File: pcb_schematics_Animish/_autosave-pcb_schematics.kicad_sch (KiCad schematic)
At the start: 73 parts, among them J1 CUE_SJ1-352XNG, J2 Conn_01x01_Pin, J3 Conn_01x05, J4 Conn_01x05, J5 Conn_01x05, SW1 SW_Push, U1 RPi_Pico_TH, U2 RDA5807M_Module, U3 LM386, U4 LM386

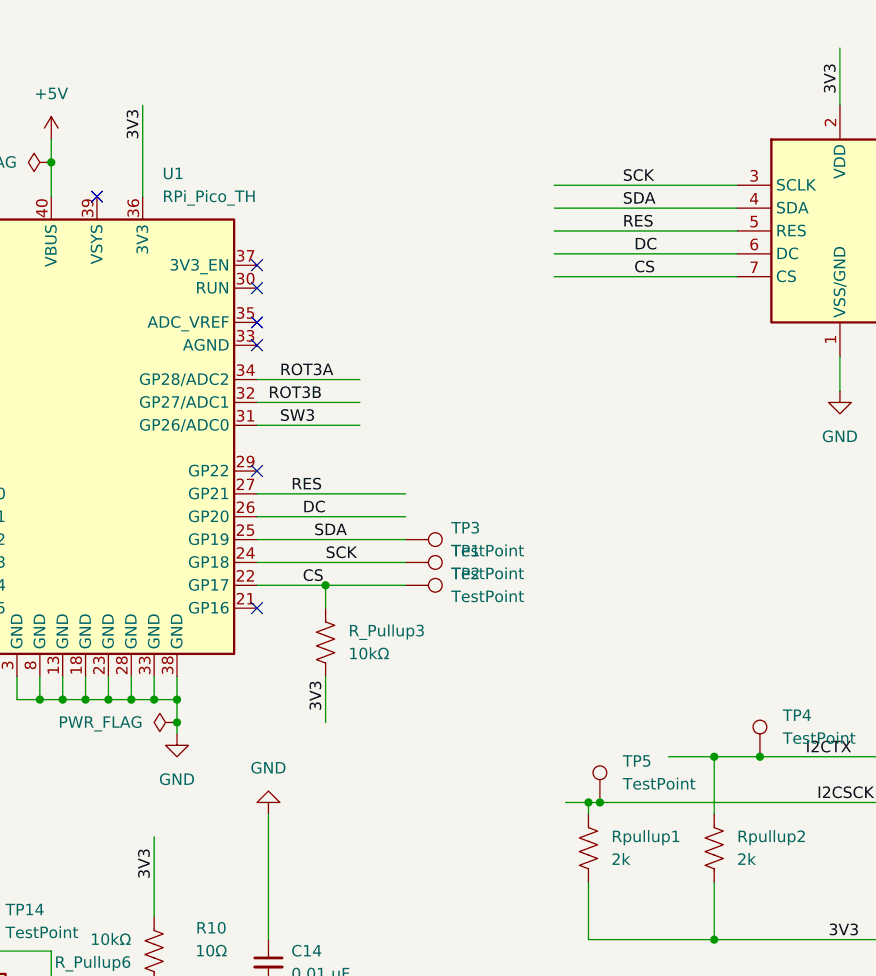
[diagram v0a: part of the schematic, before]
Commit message: Submitted to JLCPCB
Modification with pcb_schematics being the final version.
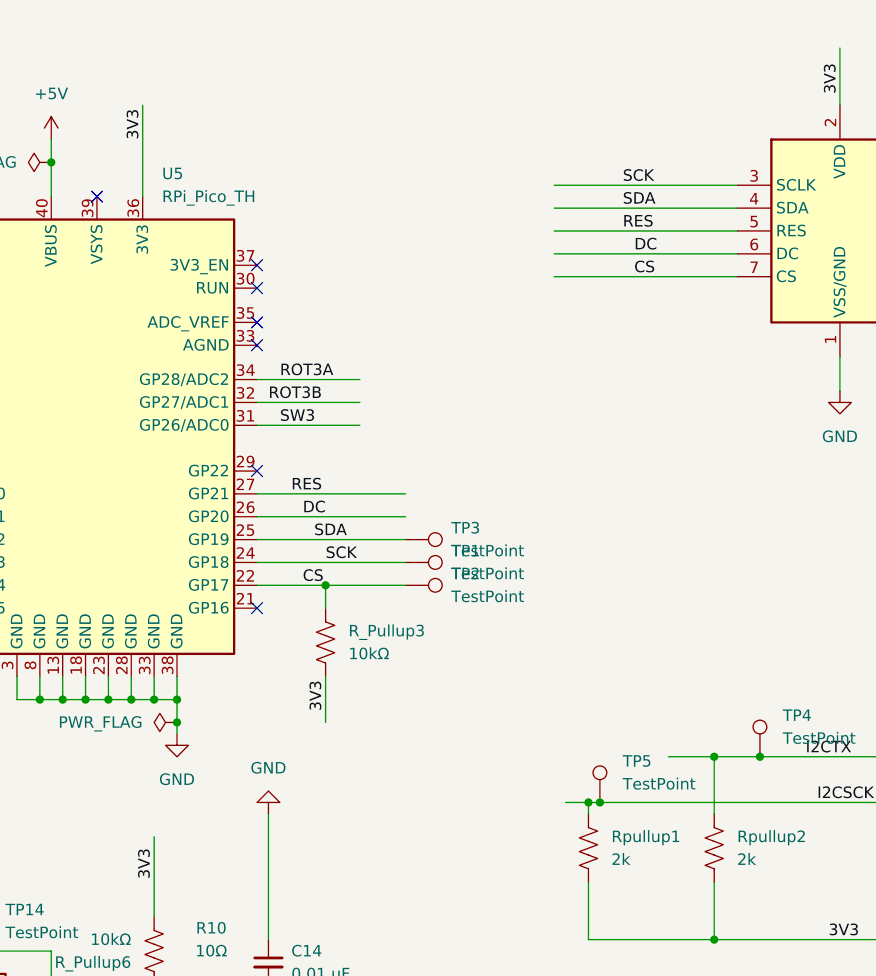
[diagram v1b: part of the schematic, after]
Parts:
- removed U1: RPi_Pico_TH, Module:RaspberryPi_Pico_Common_THT, symbol ECE:RPi_Pico_TH
- added U5: RPi_Pico_TH, ECE:RPi_Pico_TH, symbol ECE:RPi_Pico_TH
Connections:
- net +5V: now also U5.40 (VBUS)
- net 3V3: now also U5.36 (3V3)
- net CS: now also U5.22 (GP17)
- net DC: now also U5.26 (GP20)
- net GND: now also U5.13 (GND), U5.18 (GND), U5.23 (GND), U5.28 (GND), U5.3 (GND), U5.33 (AGND), U5.38 (GND), U5.8 (GND)
- net I2CSCK: now also U5.20 (GP15)
- net I2CTX: now also U5.19 (GP14)
- net RES: now also U5.27 (GP21)
- net ROT1A: now also U5.5 (GP3)
- net ROT1B: now also U5.4 (GP2)
- net ROT2A: now also U5.9 (GP6)
- net ROT2B: now also U5.10 (GP7)
- net ROT3A: now also U5.34 (GP28/ADC2)
- net ROT3B: now also U5.32 (GP27/ADC1)
- net SCK: now also U5.24 (GP18)
- net SDA: now also U5.25 (GP19)
- net SW1: now also U5.1 (GP0)
- net SW2: now also U5.2 (GP1)
- net SW3: now also U5.31 (GP26/ADC0)
- net SW4: now also U5.7 (GP5)
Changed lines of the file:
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@@
 	(wire
 		(pts
-			(xy 114.3 101.6) (xy 114.3 95.25)
+			(xy 114.3 95.25) (xy 114.3 101.6)
 		)
 		(stroke
@@
 	)
 	(symbol
-		(lib_id "ECE:RPi_Pico_TH")
-		(at 45.72 59.69 0)
-		(unit 1)
-		(exclude_from_sim no)
-		(in_bom yes)
-		(on_board yes)
-		(dnp no)
-		(fields_autoplaced yes)
-		(property "Reference" "U1"
-			(at 52.9941 30.48 0)
-			(effects
-				(font
-					(size 1.27 1.27)
-				)
-				(justify left)
-			)
-		)
-		(property "Value" "RPi_Pico_TH"
-			(at 52.9941 33.02 0)
-			(effects
-				(font
-					(size 1.27 1.27)
-				)
-				(justify left)
-			)
-		)
-		(property "Footprint" "Module:RaspberryPi_Pico_Common_THT"
-			(at 45.72 63.5 0)
-			(effects
-				(font
-					(size 1.27 1.27)
-				)
-				(hide yes)
-			)
-		)
-		(property "Datasheet" ""
-			(at 45.72 62.23 0)
-			(effects
-				(font
-					(size 1.27 1.27)
-				)
-				(hide yes)
-			)
-		)
-		(property "Description" ""
-			(at 45.72 59.69 0)
-			(effects
-				(font
-					(size 1.27 1.27)
-				)
-			)
-		)
-		(pin "34"
-		)
-		(pin "38"
-		)
-		(pin "2"
-		)
-		(pin "33"
-		)
-		(pin "37"
-		)
-		(pin "22"
-		)
-		(pin "21"
-		)
-		(pin "6"
-		)
-		(pin "8"
-		)
-		(pin "27"
-		)
-		(pin "20"
-		)
-		(pin "11"
-		)
-		(pin "25"
-		)
-		(pin "30"
-		)
-		(pin "9"
-		)
-		(pin "32"
-		)
-		(pin "33"
-		)
-		(pin "35"
-		)
-		(pin "12"
-		)
-		(pin "36"
-		)
-		(pin "31"
-		)
-		(pin "23"
-		)
-		(pin "28"
-		)
-		(pin "29"
-		)
-		(pin "5"
-		)
-		(pin "16"
-		)
-		(pin "13"
-		)
-		(pin "15"
-		)
-		(pin "39"
-		)
-		(pin "4"
-		)
-		(pin "3"
-		)
-		(pin "40"
-		)
-		(pin "17"
-		)
-		(pin "24"
-		)
-		(pin "26"
-		)
-		(pin "19"
-		)
-		(pin "1"
-		)
-		(pin "10"
-		)
-		(pin "18"
-		)
-		(pin "7"
-		)
-		(pin "14"
-		)
-		(instances
-			(project "pcb_schematics"
-				(path "/a6913523-cf8b-4e29-b403-fe0fb62af3ee"
-					(reference "U1")
-					(unit 1)
-				)
-			)
-		)
-	)
-	(symbol
 		(lib_id "Device:C_Small")
 		(at 233.68 102.87 0)
@@
 					(unit 1)
 				)
+			)
+		)
+	)
+	(symbol
+		(lib_name "RPi_Pico_TH_1")
+		(lib_id "ECE:RPi_Pico_TH")
+		(at 45.72 59.69 0)
+		(unit 1)
+		(exclude_from_sim no)
+		(in_bom yes)
+		(on_board yes)
+		(dnp no)
+		(fields_autoplaced yes)
+		(property "Reference" "U5"
+			(at 52.9433 30.48 0)
+			(effects
+				(font
+					(size 1.27 1.27)
+				)
+				(justify left)
+			)
+		)
+		(property "Value" "RPi_Pico_TH"
+			(at 52.9433 33.02 0)
+			(effects
+				(font
+					(size 1.27 1.27)
+				)
+				(justify left)
+			)
+		)
+		(property "Footprint" "ECE:RPi_Pico_TH"
+			(at 45.72 63.5 0)
+			(effects
+				(font
+					(size 1.27 1.27)
+				)
+				(hide yes)
+			)
+		)
+		(property "Datasheet" ""
+			(at 45.72 62.23 0)
+			(effects
+				(font
+					(size 1.27 1.27)
+				)
+				(hide yes)
+			)
+		)
+		(property "Description" "Raspberry Pi Pico"
+			(at 45.72 59.69 0)
+			(effects
+				(font
+					(size 1.27 1.27)
+				)
+				(hide yes)
+			)
+		)
+		(pin "6"
+		)
+		(pin "11"
+		)
+		(pin "2"
+		)
+		(pin "13"
+		)
+		(pin "19"
+		)
+		(pin "17"
+		)
+		(pin "33"
+		)
+		(pin "5"
+		)
+		(pin "7"
+		)
+		(pin "12"
+		)
+		(pin "9"
+		)
+		(pin "14"
+		)
+		(pin "16"
+		)
+		(pin "20"
+		)
+		(pin "8"
+		)
+		(pin "23"
+		)
+		(pin "28"
+		)
+		(pin "1"
+		)
+		(pin "4"
+		)
+		(pin "10"
+		)
+		(pin "15"
+		)
+		(pin "3"
+		)
+		(pin "40"
+		)
+		(pin "18"
+		)
+		(pin "36"
+		)
+		(pin "39"
+		)
+		(pin "21"
+		)
+		(pin "35"
+		)
+		(pin "29"
+		)
+		(pin "37"
+		)
+		(pin "26"
+		)
+		(pin "31"
+		)
+		(pin "25"
+		)
+		(pin "33"
+		)
+		(pin "38"
+		)
+		(pin "24"
+		)
+		(pin "32"
+		)
+		(pin "27"
+		)
+		(pin "30"
+		)
+		(pin "34"
+		)
+		(pin "22"
+		)
+		(instances
+			(project ""
+				(path "/a6913523-cf8b-4e29-b403-fe0fb62af3ee"
+					(reference "U5")
+					(unit 1)
+				)
